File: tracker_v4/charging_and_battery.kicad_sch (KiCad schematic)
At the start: 20 parts, among them J1 USB_C_Receptacle_PowerOnly_6P, Q1 DMG9926UDM-7, U3 DW01A, U5 TP4056-42-ESOP8

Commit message: starting v4
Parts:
- removed J1: USB_C_Receptacle_PowerOnly_6P, Connector_USB:USB_C_Receptacle_GCT_USB4125-xx-x-0190_6P_TopMnt_Horizontal, symbol Connector:USB_C_Receptacle_PowerOnly_6P
- added J1: USB_C_Receptacle_USB2.0_16P, symbol Connector:USB_C_Receptacle_USB2.0_16P
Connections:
- net PROTECT_MID is gone; now on net BAT-: Q1.2, Q1.5, R9.2
- net BAT-: now also C7.1, R7.2, U3.5 (VCC)
- net GND: now also J1.A1 (GND), J1.A12 (GND), J1.B1 (GND), J1.B12 (GND), J1.SH (SHIELD)
- net USB_VBUS: now also J1.A4 (VBUS), J1.A9 (VBUS), J1.B4 (VBUS), J1.B9 (VBUS)
- net at R5.1: now also J1.B5 (CC2)
- net at R6.1: now also J1.A5 (CC1)
- new net USB_DM: J1.A6 (D+), J1.B6 (D+)
- new net USB_DP: J1.A7 (D-), J1.B7 (D-)
- no-connect marks 0 -> 2
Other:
- moved on the sheet: BT1, C7, D1, D2, R10, R5, R7, R8, TP8

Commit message: added some stuff to schematic
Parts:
- R4: value 1.2k -> 2.1k
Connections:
- net USB_DM: now also J1.A7 (D-), J1.B7 (D-); no longer J1.A6 (D+), J1.B6 (D+)
- net USB_DP: now also J1.A6 (D+), J1.B6 (D+); no longer J1.A7 (D-), J1.B7 (D-)
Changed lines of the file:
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@@
+	)
+	(junction
+		(at 48.26 96.52)
+		(diameter 0)
+		(color 0 0 0 0)
+	)
+	(junction
+		(at 48.26 91.44)
+		(diameter 0)
+		(color 0 0 0 0)
 	)
 	(junction
@@
 	)
 	(junction
-		(at 181.61 120.65)
-		(diameter 0)
-		(color 0 0 0 0)
-	)
-	(junction
 		(at 172.72 82.55)
 		(diameter 0)
@@
 	(wire
 		(pts
-			(xy 48.26 95.25) (xy 48.26 97.79)
+			(xy 48.26 96.52) (xy 49.53 96.52)
+		)
+		(stroke
+			(width 0)
+			(type default)
+		)
+	)
+	(wire
+		(pts
+			(xy 48.26 95.25) (xy 48.26 96.52)
 		)
 		(stroke
@@
 	(wire
 		(pts
+			(xy 48.26 96.52) (xy 48.26 97.79)
+		)
+		(stroke
+			(width 0)
+			(type default)
+		)
+	)
+	(wire
+		(pts
+			(xy 48.26 97.79) (xy 46.99 97.79)
+		)
+		(stroke
+			(width 0)
+			(type default)
+		)
+	)
+	(wire
+		(pts
 			(xy 52.07 63.5) (xy 52.07 62.23)
 		)
@@
 	(wire
 		(pts
+			(xy 48.26 91.44) (xy 48.26 92.71)
+		)
+		(stroke
+			(width 0)
+			(type default)
+		)
+	)
+	(wire
+		(pts
 			(xy 46.99 173.99) (xy 46.99 163.83)
 		)
@@
 	(wire
 		(pts
-			(xy 48.26 92.71) (xy 48.26 90.17)
+			(xy 48.26 90.17) (xy 48.26 91.44)
 		)
 		(stroke
@@
 	(wire
 		(pts
-			(xy 181.61 132.08) (xy 181.61 120.65)
-		)
-		(stroke
-			(width 0)
-			(type default)
-		)
-	)
-	(wire
-		(pts
 			(xy 46.99 92.71) (xy 48.26 92.71)
 		)
@@
 	(wire
 		(pts
-			(xy 48.26 97.79) (xy 46.99 97.79)
-		)
-		(stroke
-			(width 0)
-			(type default)
-		)
-	)
-	(wire
-		(pts
 			(xy 49.53 55.88) (xy 52.07 55.88)
 		)
@@
 	(wire
 		(pts
-			(xy 50.8 146.05) (xy 50.8 85.09)
+			(xy 50.8 85.09) (xy 50.8 146.05)
 		)
 		(stroke
@@
 		(pts
 			(xy 185.42 93.98) (xy 185.42 87.63)
+		)
+		(stroke
+			(width 0)
+			(type default)
+		)
+	)
+	(wire
+		(pts
+			(xy 48.26 91.44) (xy 49.53 91.44)
 		)
 		(stroke
@@
 	(hierarchical_label "USB_DM"
 		(shape output)
-		(at 48.26 97.79 0)
+		(at 49.53 91.44 0)
 		(effects
 			(font
@@
 	(hierarchical_label "USB_DP"
 		(shape output)
-		(at 48.26 91.44 0)
+		(at 49.53 96.52 0)
 		(effects
 			(font
@@
 			)
 		)
-		(property "Value" "1.2k"
+		(property "Value" "2.1k"
 			(at 93.98 121.9199 0)
 			(show_name no)

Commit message: m
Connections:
- net BAT-: no longer C7.1, Q1.1, Q1.2, Q1.5, R7.2, R9.2, U3.5 (VCC)
- net PROTECT_MID: now reaches Q1.6, U3.1 (OD)
- net PROTECT_MID: now also Q1.2, Q1.5, R9.2
- new net: C7.1, R7.2, U3.5 (VCC)
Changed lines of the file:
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@@
+	)
+	(junction
+		(at 209.55 115.57)
+		(diameter 0)
+		(color 0 0 0 0)
 	)
 	(junction
@@
 	)
 	(junction
-		(at 184.15 120.65)
-		(diameter 0)
-		(color 0 0 0 0)
-	)
-	(junction
-		(at 129.54 128.27)
-		(diameter 0)
-		(color 0 0 0 0)
-	)
-	(junction
 		(at 222.25 118.11)
 		(diameter 0)
@@
 	)
 	(junction
+		(at 147.32 81.28)
+		(diameter 0)
+		(color 0 0 0 0)
+	)
+	(junction
 		(at 31.75 163.83)
 		(diameter 0)
@@
 	)
 	(junction
-		(at 172.72 82.55)
-		(diameter 0)
-		(color 0 0 0 0)
-	)
-	(junction
 		(at 67.31 78.74)
 		(diameter 0)
@@
 	)
 	(junction
-		(at 160.02 123.19)
-		(diameter 0)
-		(color 0 0 0 0)
-	)
-	(junction
 		(at 129.54 114.3)
 		(diameter 0)
@@
 	)
 	(junction
-		(at 147.32 83.82)
-		(diameter 0)
-		(color 0 0 0 0)
-	)
-	(junction
 		(at 101.6 90.17)
+		(diameter 0)
+		(color 0 0 0 0)
+	)
+	(junction
+		(at 222.25 115.57)
 		(diameter 0)
 		(color 0 0 0 0)
@@
 	(wire
 		(pts
-			(xy 160.02 134.62) (xy 160.02 123.19)
-		)
-		(stroke
-			(width 0)
-			(type default)
-		)
-	)
-	(wire
-		(pts
-			(xy 172.72 82.55) (xy 172.72 77.47)
-		)
-		(stroke
-			(width 0)
-			(type default)
-		)
-	)
-	(wire
-		(pts
-			(xy 160.02 81.28) (xy 160.02 123.19)
+			(xy 147.32 81.28) (xy 147.32 90.17)
 		)
 		(stroke
@@
 	(wire
 		(pts
-			(xy 129.54 134.62) (xy 129.54 128.27)
-		)
-		(stroke
-			(width 0)
-			(type default)
-		)
-	)
-	(wire
-		(pts
 			(xy 64.77 106.68) (xy 64.77 113.03)
 		)
@@
 	(wire
 		(pts
+			(xy 147.32 77.47) (xy 147.32 81.28)
+		)
+		(stroke
+			(width 0)
+			(type default)
+		)
+	)
+	(wire
+		(pts
 			(xy 55.88 134.62) (xy 55.88 163.83)
 		)
@@
 	(wire
 		(pts
-			(xy 184.15 123.19) (xy 184.15 120.65)
-		)
-		(stroke
-			(width 0)
-			(type default)
-		)
-	)
-	(wire
-		(pts
 			(xy 52.07 55.88) (xy 52.07 54.61)
 		)
@@
 	(wire
 		(pts
-			(xy 181.61 120.65) (xy 181.61 113.03)
-		)
-		(stroke
-			(width 0)
-			(type default)
-		)
-	)
-	(wire
-		(pts
-			(xy 129.54 127) (xy 129.54 128.27)
+			(xy 181.61 120.65) (xy 181.61 115.57)
 		)
 		(stroke
@@
 	(wire
 		(pts
-			(xy 181.61 113.03) (xy 222.25 113.03)
+			(xy 181.61 115.57) (xy 209.55 115.57)
 		)
 		(stroke
@@
 	(wire
 		(pts
-			(xy 147.32 83.82) (xy 172.72 83.82)
-		)
-		(stroke
-			(width 0)
-			(type default)
-		)
-	)
-	(wire
-		(pts
 			(xy 55.88 96.52) (xy 55.88 127)
 		)
@@
 	(wire
 		(pts
+			(xy 172.72 77.47) (xy 147.32 77.47)
+		)
+		(stroke
+			(width 0)
+			(type default)
+		)
+	)
+	(wire
+		(pts
 			(xy 129.54 134.62) (xy 147.32 134.62)
 		)
@@
 	(wire
 		(pts
-			(xy 160.02 81.28) (xy 154.94 81.28)
-		)
-		(stroke
-			(width 0)
-			(type default)
-		)
-	)
-	(wire
-		(pts
 			(xy 76.2 113.03) (xy 78.74 113.03)
 		)
@@
 	(wire
 		(pts
-			(xy 154.94 81.28) (xy 154.94 82.55)
-		)
-		(stroke
-			(width 0)
-			(type default)
-		)
-	)
-	(wire
-		(pts
 			(xy 50.8 85.09) (xy 50.8 146.05)
 		)
@@
 	(wire
 		(pts
-			(xy 172.72 83.82) (xy 172.72 82.55)
+			(xy 160.02 82.55) (xy 172.72 82.55)
+		)
+		(stroke
+			(width 0)
+			(type default)
+		)
+	)
+	(wire
+		(pts
+			(xy 209.55 115.57) (xy 222.25 115.57)
 		)
 		(stroke
@@
 	(wire
 		(pts
-			(xy 184.15 120.65) (xy 184.15 113.03)
-		)
-		(stroke
-			(width 0)
-			(type default)
-		)
-	)
-	(wire
-		(pts
-			(xy 154.94 82.55) (xy 172.72 82.55)
-		)
-		(stroke
-			(width 0)
-			(type default)
-		)
-	)
-	(wire
-		(pts
 			(xy 172.72 144.78) (xy 184.15 144.78)
 		)
@@
 	(wire
 		(pts
+			(xy 129.54 128.27) (xy 129.54 134.62)
+		)
+		(stroke
+			(width 0)
+			(type default)
+		)
+	)
+	(wire
+		(pts
 			(xy 129.54 97.79) (xy 129.54 105.41)
 		)
@@
 	(wire
 		(pts
-			(xy 147.32 83.82) (xy 147.32 90.17)
-		)
-		(stroke
-			(width 0)
-			(type default)
-		)
-	)
-	(wire
-		(pts
 			(xy 67.31 78.74) (xy 78.74 78.74)
 		)
@@
 	(wire
 		(pts
-			(xy 222.25 113.03) (xy 222.25 118.11)
-		)
-		(stroke
-			(width 0)
-			(type default)
-		)
-	)
-	(wire
-		(pts
-			(xy 209.55 115.57) (xy 228.6 115.57)
+			(xy 222.25 115.57) (xy 222.25 118.11)
 		)
 		(stroke
@@
 	(wire
 		(pts
-			(xy 147.32 81.28) (xy 147.32 83.82)
-		)
-		(stroke
-			(width 0)
-			(type default)
-		)
-	)
-	(wire
-		(pts
 			(xy 228.6 96.52) (xy 180.34 96.52)
 		)
@@
 	(wire
 		(pts
+			(xy 222.25 115.57) (xy 228.6 115.57)
+		)
+		(stroke
+			(width 0)
+			(type default)
+		)
+	)
+	(wire
+		(pts
 			(xy 76.2 107.95) (xy 76.2 113.03)
 		)
@@
 	(wire
 		(pts
-			(xy 160.02 123.19) (xy 184.15 123.19)
-		)
-		(stroke
-			(width 0)
-			(type default)
-		)
-	)
-	(wire
-		(pts
 			(xy 91.44 129.54) (xy 91.44 134.62)
 		)
@@
 	(wire
 		(pts
+			(xy 160.02 82.55) (xy 160.02 134.62)
+		)
+		(stroke
+			(width 0)
+			(type default)
+		)
+	)
+	(wire
+		(pts
 			(xy 59.69 34.29) (xy 59.69 30.48)
 		)
@@
 	)
 	(label "PROTECT_MID"
-		(at 205.74 113.03 0)
+		(at 205.74 115.57 0)
 		(effects
 			(font

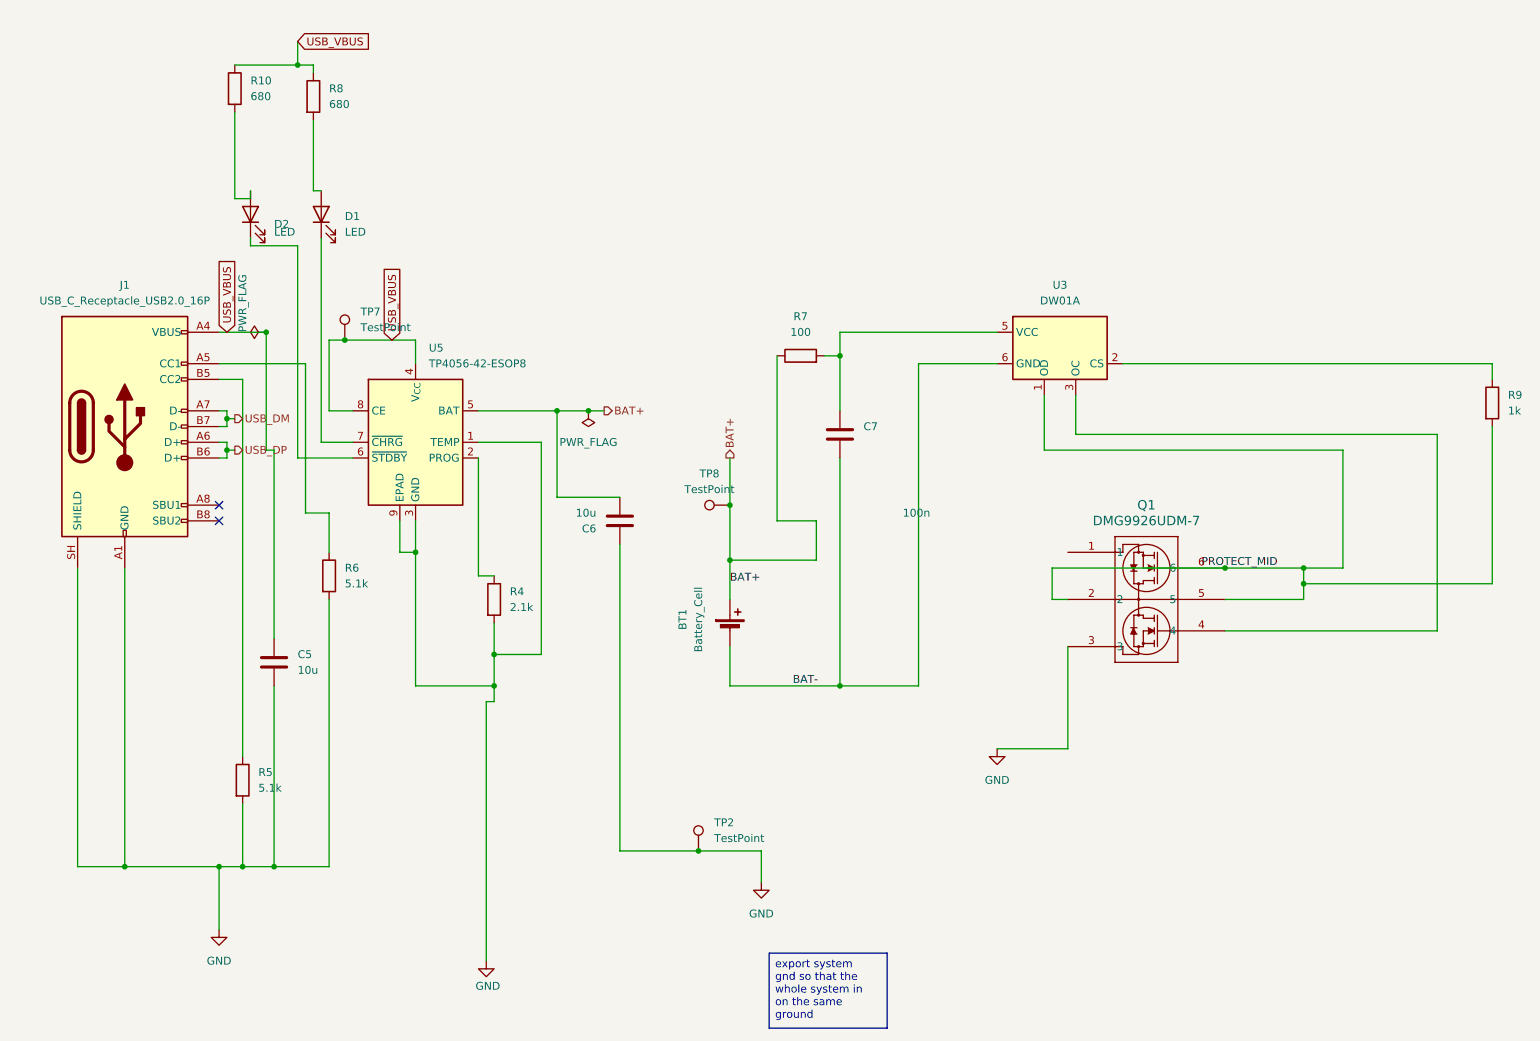
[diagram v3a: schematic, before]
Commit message: added diodes
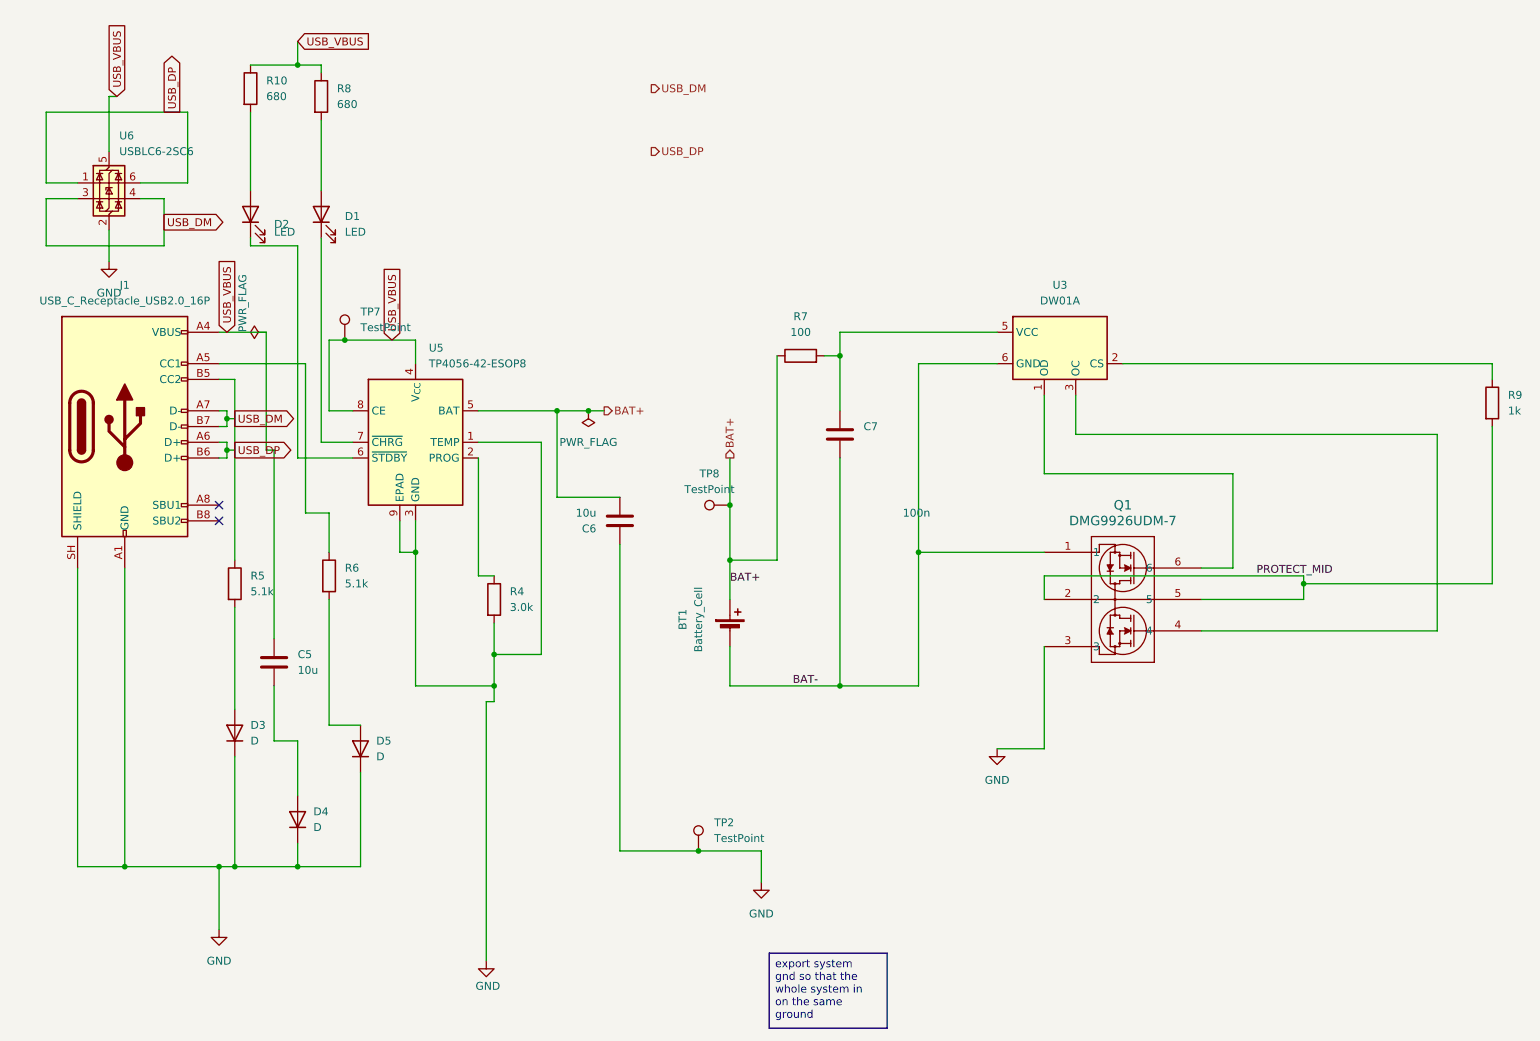
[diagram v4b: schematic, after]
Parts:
- added D3, D4, D5: D, Diode_SMD:D_SOD-123F, symbol Device:D
- added U6: USBLC6-2SC6, Package_TO_SOT_SMD:SOT-23-6, symbol Power_Protection:USBLC6-2SC6
- J1: footprint (none) -> Connector_USB:USB_C_Receptacle_GCT_USB4105-xx-A_16P_TopMnt_Horizontal
- R4: value 2.1k -> 3.0k
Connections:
- net USB_DP is gone; now on net USB_DM: J1.A6 (D+), J1.B6 (D+)
- net BAT-: now also Q1.1
- net GND: now also D3.1 (K), D4.1 (K), D5.1 (K), U6.2 (GND); no longer C5.2, R5.2, R6.2
- net PROTECT_MID: no longer Q1.6, U3.1 (OD)
- net USB_DM: now also J1.B5 (CC2), R5.1, U6.1 (I/O1), U6.3 (I/O2), U6.4 (I/O2), U6.6 (I/O1)
- net USB_VBUS: now also U6.5 (VBUS)
- new net: C5.2, D4.2 (A)
- new net: D3.2 (A), R5.2
- new net: D5.2 (A), R6.2
- new net: Q1.6, U3.1 (OD)
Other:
- moved on the sheet: Q1, R10, R5, R8
